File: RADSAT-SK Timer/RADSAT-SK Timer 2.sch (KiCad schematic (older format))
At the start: 34 parts, among them J201 Conn_01x07, J202 Conn_01x05, J203 Conn_01x02, J204 Conn_01x02, J205 Conn_01x02, J206 Conn_01x02, J210 ZX62WRD-B-5PC, Q201 IRLML2060, Q202 IRLML2060, SW201 SW_Push, SW202 SW_Push, SW203 SW_Push, SW204 SW_Push, SW205 SW_Push, SW206 SW_Push, U202 LTC3440EMSPBF

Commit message: More Library management, added text to pcb to identify easily connectors, Added a cool custom USST RADSAT-SK Logo to the project, may need to be scaled down or placed on back of board
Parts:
- J203: value Conn_01x02 -> Conn_01x03; footprint Connector_Hirose:Hirose_DF13-02P-1.25DSA_1x02_P1.25mm_Vertical -> Connector_Hirose:Hirose_DF13-03P-1.25DSA_1x03_P1.25mm_Vertical; symbol Connector_Generic:Conn_01x02 -> Connector_Generic:Conn_01x03
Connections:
- wire segments 132 -> 131
- no-connect marks 4 -> 5
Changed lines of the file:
@@
 	4825 1625 4825 1450
 Wire Wire Line
-	4825 1450 6325 1450
+	4825 1450 6300 1450
 Connection ~ 4825 1625
 Wire Wire Line
@@
 	4500 4150 4800 4150
 Wire Wire Line
-	6325 1450 6325 1850
-Wire Wire Line
-	6300 1850 6325 1850
-Connection ~ 6325 1850
-Wire Wire Line
-	6325 1850 7700 1850
+	6300 1450 6300 1850
 Wire Wire Line
 	4800 3225 4800 3500
@@
 $EndComp
 $Comp
-L Connector_Generic:Conn_01x02 J203
+L Connector_Generic:Conn_01x03 J203
 U 1 1 615188F9
-P 4300 5525
-F 0 "J203" H 4380 5517 50  0000 L CNN
-F 1 "Conn_01x02" H 4380 5426 50  0000 L CNN
-F 2 "Connector_Hirose:Hirose_DF13-02P-1.25DSA_1x02_P1.25mm_Vertical" H 4300 5525 50  0001 C CNN
-F 3 "~" H 4300 5525 50  0001 C CNN
-	1    4300 5525
+P 4300 5625
+F 0 "J203" H 4380 5617 50  0000 L CNN
+F 1 "Conn_01x03" H 4380 5526 50  0000 L CNN
+F 2 "Connector_Hirose:Hirose_DF13-03P-1.25DSA_1x03_P1.25mm_Vertical" H 4300 5625 50  0001 C CNN
+F 3 "~" H 4300 5625 50  0001 C CNN
+	1    4300 5625
 	1    0    0    -1
 $EndComp
@@
 Wire Wire Line
 	1300 5900 1300 6025
+NoConn ~ 4100 5725
+Connection ~ 6300 1850
+Wire Wire Line
+	6300 1850 7700 1850
 $EndSCHEMATC

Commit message: JFET
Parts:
- added Q203: PJFET, Package_TO_SOT_THT:TO-92L_Inline_Wide, symbol Device:Q_PJFET_DGS
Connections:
- wire segments 131 -> 135
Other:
- moved on the sheet: J203
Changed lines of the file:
@@
 L Connector_Generic:Conn_01x03 J203
 U 1 1 615188F9
-P 4300 5625
-F 0 "J203" H 4380 5617 50  0000 L CNN
-F 1 "Conn_01x03" H 4380 5526 50  0000 L CNN
-F 2 "Connector_Hirose:Hirose_DF13-03P-1.25DSA_1x03_P1.25mm_Vertical" H 4300 5625 50  0001 C CNN
-F 3 "~" H 4300 5625 50  0001 C CNN
-	1    4300 5625
+P 4375 5375
+F 0 "J203" H 4455 5367 50  0000 L CNN
+F 1 "Conn_01x03" H 4455 5276 50  0000 L CNN
+F 2 "Connector_Hirose:Hirose_DF13-03P-1.25DSA_1x03_P1.25mm_Vertical" H 4375 5375 50  0001 C CNN
+F 3 "~" H 4375 5375 50  0001 C CNN
+	1    4375 5375
 	1    0    0    -1
 $EndComp
@@
 	1    0    0    -1
 $EndComp
-$Comp
-L power:GND #PWR0119
-U 1 1 61557785
-P 3900 5800
-F 0 "#PWR0119" H 3900 5550 50  0001 C CNN
-F 1 "GND" H 3905 5627 50  0000 C CNN
-F 2 "" H 3900 5800 50  0001 C CNN
-F 3 "" H 3900 5800 50  0001 C CNN
-	1    3900 5800
-	1    0    0    -1
-$EndComp
 Wire Wire Line
 	5475 6500 4625 6500
@@
 Text Notes 2175 5125 0    50   ~ 0
 RBF Logic for Batt Board Inhibit
-Wire Wire Line
-	3125 5425 3125 5525
-Wire Wire Line
-	3900 5800 3900 5625
-Wire Wire Line
-	3900 5625 4100 5625
-Wire Wire Line
-	4100 5525 3125 5525
-Connection ~ 3125 5525
-Wire Wire Line
-	3125 5525 3125 5700
 Wire Notes Line
 	4925 5000 4925 6300
@@
 Wire Wire Line
 	1300 5900 1300 6025
-NoConn ~ 4100 5725
+NoConn ~ 4175 5475
 Connection ~ 6300 1850
 Wire Wire Line
 	6300 1850 7700 1850
+$Comp
+L Device:Q_PJFET_DGS Q203
+U 1 1 6167F061
+P 3475 5525
+F 0 "Q203" H 3665 5571 50  0000 L CNN
+F 1 "PJFET" H 3665 5480 50  0000 L CNN
+F 2 "Package_TO_SOT_THT:TO-92L_Inline_Wide" H 3675 5625 50  0001 C CNN
+F 3 "~" H 3475 5525 50  0001 C CNN
+	1    3475 5525
+	1    0    0    -1
+$EndComp
+Wire Wire Line
+	3125 5425 3125 5525
+Wire Wire Line
+	3275 5525 3125 5525
+Connection ~ 3125 5525
+Wire Wire Line
+	3125 5525 3125 5700
+Wire Wire Line
+	3575 5325 3575 5275
+Wire Wire Line
+	3575 5275 4175 5275
+Wire Wire Line
+	4175 5375 4075 5375
+Wire Wire Line
+	4075 5775 3575 5775
+Wire Wire Line
+	3575 5775 3575 5725
+Wire Wire Line
+	4075 5375 4075 5775
 $EndSCHEMATC

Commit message: added pchannel JFET and Diode logic for inhibitors, edited the layout a bit still not final
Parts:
- added D206: D, Diode_SMD:D_0805_2012Metric, symbol Device:D
- added Q204, Q205, Q206: PJFET, Package_TO_SOT_THT:TO-92L_Inline_Wide, symbol Device:Q_PJFET_DGS
- added R204, R209, R210, R211, R212: 100, Resistor_SMD:R_0805_2012Metric, symbol Device:R
- renumbered R220 to R201, R221 to R202, R205 to R203, R209 to R205, R211 to R206, R212 to R207, R213 to R208
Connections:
- wire segments 135 -> 149
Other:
- moved on the sheet: D204, D205, J203, J204, J205, J206, Q201, Q203

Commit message: More components to the BOM and fixed footprints on the schematic to mathc chosen parts
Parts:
- C208: footprint Capacitor_SMD:C_0805_2012Metric -> Capacitor_SMD:C_1210_3225Metric_Pad1.33x2.70mm_HandSolder
- D203: value MBRM1020T3 -> MBRM120LT3G; footprint Diode_SMD:D_SOD-123F -> Diode_SMD:D_Powermite_AK; symbol Diode:MBR1020VL -> Device:D_Schottky
- D204, D205, D206: value D -> SM5817PL-TP; footprint Diode_SMD:D_0805_2012Metric -> Diode_SMD:D_SOD-123
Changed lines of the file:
@@
 Wire Wire Line
 	6300 2025 6300 1850
-$Comp
-L Diode:MBR1020VL D203
-U 1 1 60121A1E
-P 9400 1425
-AR Path="/60121A1E" Ref="D203"  Part="1"
-AR Path="/602E25D3/60121A1E" Ref="D203"  Part="1"
-F 0 "D203" H 9400 1209 50  0000 C CNN
-F 1 "MBRM1020T3" H 9400 1300 50  0000 C CNN
-F 2 "Diode_SMD:D_SOD-123F" H 9400 1250 50  0001 C CNN
-F 3 "https://www.onsemi.com/pub/Collateral/MBR1020VL-D.PDF" H 9400 1425 50  0001 C CNN
-	1    9400 1425
-	-1   0    0    1
-$EndComp
 Wire Wire Line
 	9100 1425 9250 1425
@@
 F 0 "C208" H 10515 2221 50  0000 L CNN
 F 1 "22uF" H 10515 2130 50  0000 L CNN
-F 2 "Capacitor_SMD:C_0805_2012Metric" H 10438 2025 50  0001 C CNN
+F 2 "Capacitor_SMD:C_1210_3225Metric_Pad1.33x2.70mm_HandSolder" H 10438 2025 50  0001 C CNN
 F 3 "~" H 10400 2175 50  0001 C CNN
 	1    10400 2175
@@
 	2950 3300 2825 3300
 $Comp
-L Device:D D204
-U 1 1 615B7582
-P 2875 5450
-F 0 "D204" H 2875 5233 50  0000 C CNN
-F 1 "D" H 2875 5324 50  0000 C CNN
-F 2 "Diode_SMD:D_0805_2012Metric" H 2875 5450 50  0001 C CNN
-F 3 "~" H 2875 5450 50  0001 C CNN
-	1    2875 5450
-	-1   0    0    1
-$EndComp
-$Comp
 L power:+BATT #PWR0116
 U 1 1 6152A0B5
@@
 $EndComp
 $Comp
-L Device:D D205
-U 1 1 615BB367
-P 2875 5725
-F 0 "D205" H 2875 5850 50  0000 C CNN
-F 1 "D" H 2875 5925 50  0000 C CNN
-F 2 "Diode_SMD:D_0805_2012Metric" H 2875 5725 50  0001 C CNN
-F 3 "~" H 2875 5725 50  0001 C CNN
-	1    2875 5725
-	-1   0    0    1
-$EndComp
-$Comp
 L Device:Q_PJFET_DGS Q206
 U 1 1 616CA172
@@
 	1    4900 7550
 	1    0    0    -1
-$EndComp
-$Comp
-L Device:D D206
-U 1 1 617CE68C
-P 3500 7300
-F 0 "D206" H 3500 7425 50  0000 C CNN
-F 1 "D" H 3500 7500 50  0000 C CNN
-F 2 "Diode_SMD:D_0805_2012Metric" H 3500 7300 50  0001 C CNN
-F 3 "~" H 3500 7300 50  0001 C CNN
-	1    3500 7300
-	-1   0    0    1
 $EndComp
 Wire Wire Line
@@
 Wire Wire Line
 	3575 5550 3725 5550
+$Comp
+L Device:D_Schottky D203
+U 1 1 60121A1E
+P 9400 1425
+AR Path="/60121A1E" Ref="D203"  Part="1"
+AR Path="/602E25D3/60121A1E" Ref="D203"  Part="1"
+F 0 "D203" H 9400 1209 50  0000 C CNN
+F 1 "MBRM120LT3G" H 9400 1300 50  0000 C CNN
+F 2 "Diode_SMD:D_Powermite_AK" H 9400 1250 50  0001 C CNN
+F 3 "https://www.onsemi.com/pdf/datasheet/mbrm120l-d.pdf" H 9400 1425 50  0001 C CNN
+	1    9400 1425
+	-1   0    0    1
+$EndComp
+$Comp
+L Device:D D204
+U 1 1 615B7582
+P 2875 5450
+F 0 "D204" H 2875 5233 50  0000 C CNN
+F 1 "SM5817PL-TP" H 2875 5324 50  0000 C CNN
+F 2 "Diode_SMD:D_SOD-123" H 2875 5450 50  0001 C CNN
+F 3 "~https://www.mccsemi.com/pdf/Products/SM5817PL-SM5819PL(SOD-123FL).PDF" H 2875 5450 50  0001 C CNN
+	1    2875 5450
+	-1   0    0    1
+$EndComp
+$Comp
+L Device:D D205
+U 1 1 61746364
+P 2875 5725
+F 0 "D205" H 2875 5825 50  0000 C CNN
+F 1 "SM5817PL-TP" H 2875 5625 50  0000 C CNN
+F 2 "Diode_SMD:D_SOD-123" H 2875 5725 50  0001 C CNN
+F 3 "~https://www.mccsemi.com/pdf/Products/SM5817PL-SM5819PL(SOD-123FL).PDF" H 2875 5725 50  0001 C CNN
+	1    2875 5725
+	-1   0    0    1
+$EndComp
+$Comp
+L Device:D D206
+U 1 1 61747DDB
+P 3500 7300
+F 0 "D206" H 3500 7400 50  0000 C CNN
+F 1 "SM5817PL-TP" H 3500 7200 50  0000 C CNN
+F 2 "Diode_SMD:D_SOD-123" H 3500 7300 50  0001 C CNN
+F 3 "~https://www.mccsemi.com/pdf/Products/SM5817PL-SM5819PL(SOD-123FL).PDF" H 3500 7300 50  0001 C CNN
+	1    3500 7300
+	-1   0    0    1
+$EndComp
 $EndSCHEMATC

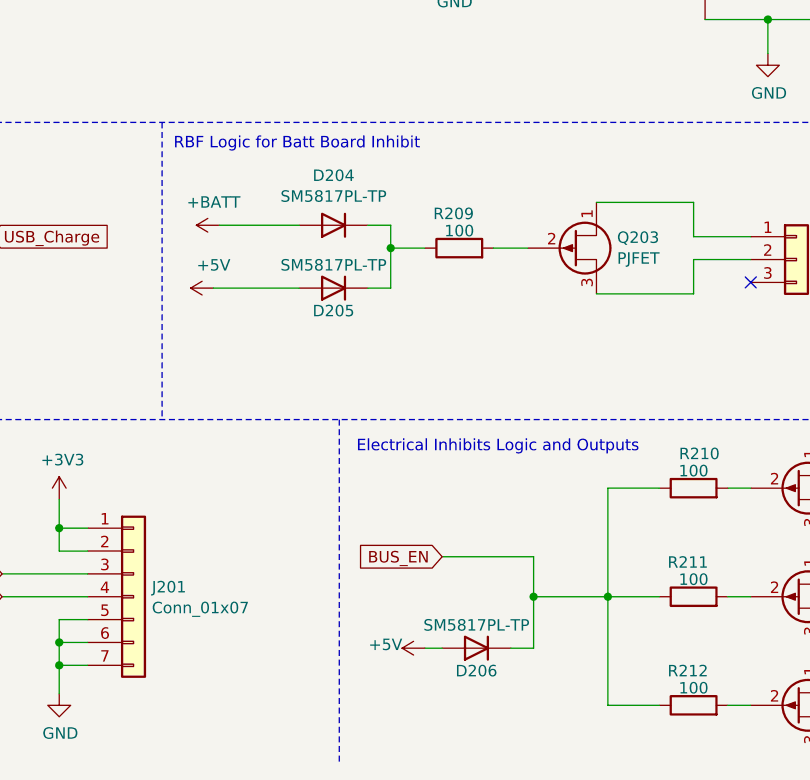
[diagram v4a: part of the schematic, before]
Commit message: This commit contains more ccomponent sourcing, mainly a diode array for the inhibitor logic diodes, handsoldering footprints have been chosen for some of the sourced components, see BOM, this should help us save time and frustration in handsoldering the testboard, SW connectors were reorganized to make better connections and now both side panels must be closed to connect the battery
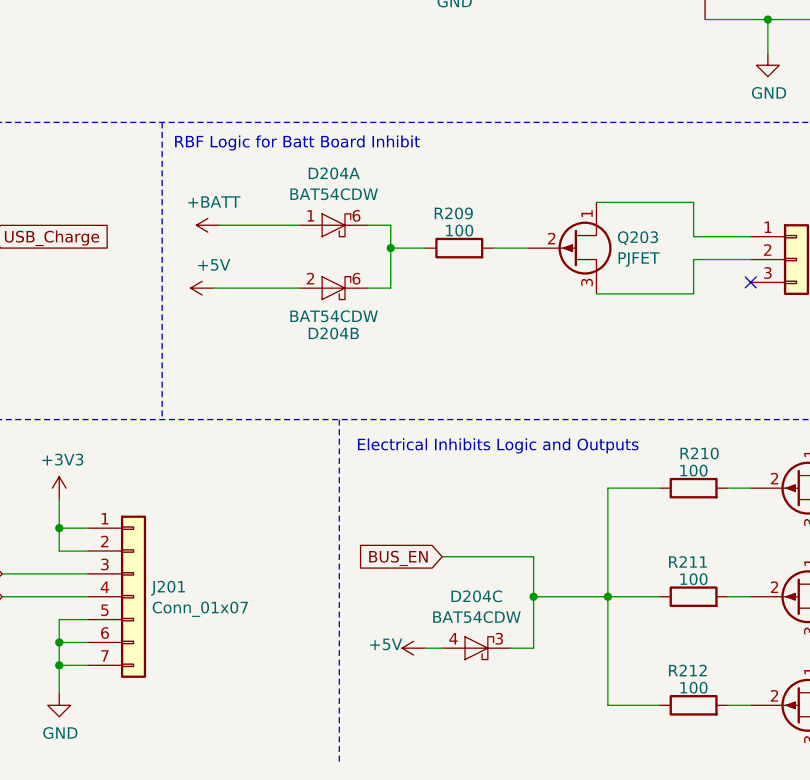
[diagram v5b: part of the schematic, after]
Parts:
- removed D204, D205, D206: SM5817PL-TP, Diode_SMD:D_SOD-123, symbol Device:D
- added D204: BAT54CDW, Package_TO_SOT_SMD:SOT-363_SC-70-6_Handsoldering, symbol BAT54CDW:BAT54CDW
- Q201, Q202: footprint Package_TO_SOT_SMD:SOT-23 -> Package_TO_SOT_SMD:SOT-23_Handsoldering
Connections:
- net +5V: now also D204.2 (A), D204.4 (A)
- net +BATT: now also D204.1 (A)
- net BUS_EN: now also D204.3 (K)
- net at R209.1: now also D204.6 (K), D204.6 (K)
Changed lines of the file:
@@
 F 0 "Q201" H 6725 2125 50  0000 L CNN
 F 1 "IRLML2060" H 6500 2200 50  0000 L CNN
-F 2 "Package_TO_SOT_SMD:SOT-23" H 7050 2250 50  0001 L CIN
+F 2 "Package_TO_SOT_SMD:SOT-23_Handsoldering" H 7050 2250 50  0001 L CIN
 F 3 "https://www.infineon.com/dgdl/irlml2060pbf.pdf?fileId=5546d462533600a401535664b7fb25ee" H 6850 2325 50  0001 L CNN
 	1    6850 2325
@@
 F 0 "Q202" H 4475 3600 50  0000 L CNN
 F 1 "IRLML2060" H 4375 3500 50  0000 L CNN
-F 2 "Package_TO_SOT_SMD:SOT-23" H 4900 3625 50  0001 L CIN
+F 2 "Package_TO_SOT_SMD:SOT-23_Handsoldering" H 4900 3625 50  0001 L CIN
 F 3 "https://www.infineon.com/dgdl/irlml2060pbf.pdf?fileId=5546d462533600a401535664b7fb25ee" H 4700 3700 50  0001 L CNN
 	1    4700 3700
@@
 $EndComp
 $Comp
-L Device:D D204
-U 1 1 615B7582
+L BAT54CDW:BAT54CDW D204
+U 1 1 6175B9D1
 P 2875 5450
-F 0 "D204" H 2875 5233 50  0000 C CNN
-F 1 "SM5817PL-TP" H 2875 5324 50  0000 C CNN
-F 2 "Diode_SMD:D_SOD-123" H 2875 5450 50  0001 C CNN
-F 3 "~https://www.mccsemi.com/pdf/Products/SM5817PL-SM5819PL(SOD-123FL).PDF" H 2875 5450 50  0001 C CNN
+F 0 "D204" H 2875 5225 50  0000 C CNN
+F 1 "BAT54CDW" H 2875 5316 50  0000 C CNN
+F 2 "Package_TO_SOT_SMD:SOT-363_SC-70-6_Handsoldering" H 2875 5275 50  0001 C CNN
+F 3 "https://www.panjit.com.tw/upload/datasheet/BAT54TW_SERIES.pdf" H 2875 5550 50  0001 C CNN
 	1    2875 5450
 	-1   0    0    1
 $EndComp
 $Comp
-L Device:D D205
-U 1 1 61746364
+L BAT54CDW:BAT54CDW D204
+U 2 1 6175E48B
 P 2875 5725
-F 0 "D205" H 2875 5825 50  0000 C CNN
-F 1 "SM5817PL-TP" H 2875 5625 50  0000 C CNN
-F 2 "Diode_SMD:D_SOD-123" H 2875 5725 50  0001 C CNN
-F 3 "~https://www.mccsemi.com/pdf/Products/SM5817PL-SM5819PL(SOD-123FL).PDF" H 2875 5725 50  0001 C CNN
-	1    2875 5725
+F 0 "D204" H 2875 5925 50  0000 C CNN
+F 1 "BAT54CDW" H 2875 5850 50  0000 C CNN
+F 2 "Package_TO_SOT_SMD:SOT-363_SC-70-6_Handsoldering" H 2875 5550 50  0001 C CNN
+F 3 "https://www.panjit.com.tw/upload/datasheet/BAT54TW_SERIES.pdf" H 2875 5825 50  0001 C CNN
+	2    2875 5725
 	-1   0    0    1
 $EndComp
 $Comp
-L Device:D D206
-U 1 1 61747DDB
+L BAT54CDW:BAT54CDW D204
+U 3 1 61760717
 P 3500 7300
-F 0 "D206" H 3500 7400 50  0000 C CNN
-F 1 "SM5817PL-TP" H 3500 7200 50  0000 C CNN
-F 2 "Diode_SMD:D_SOD-123" H 3500 7300 50  0001 C CNN
-F 3 "~https://www.mccsemi.com/pdf/Products/SM5817PL-SM5819PL(SOD-123FL).PDF" H 3500 7300 50  0001 C CNN
-	1    3500 7300
+F 0 "D204" H 3500 7075 50  0000 C CNN
+F 1 "BAT54CDW" H 3500 7166 50  0000 C CNN
+F 2 "Package_TO_SOT_SMD:SOT-363_SC-70-6_Handsoldering" H 3500 7125 50  0001 C CNN
+F 3 "https://www.panjit.com.tw/upload/datasheet/BAT54TW_SERIES.pdf" H 3500 7400 50  0001 C CNN
+	3    3500 7300
 	-1   0    0    1
 $EndComp
